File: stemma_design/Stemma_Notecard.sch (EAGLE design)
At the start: 18 parts, among them J1 MDT420E01001NOTECARD, Q2 BSS138, U2 AP2112K-3.3

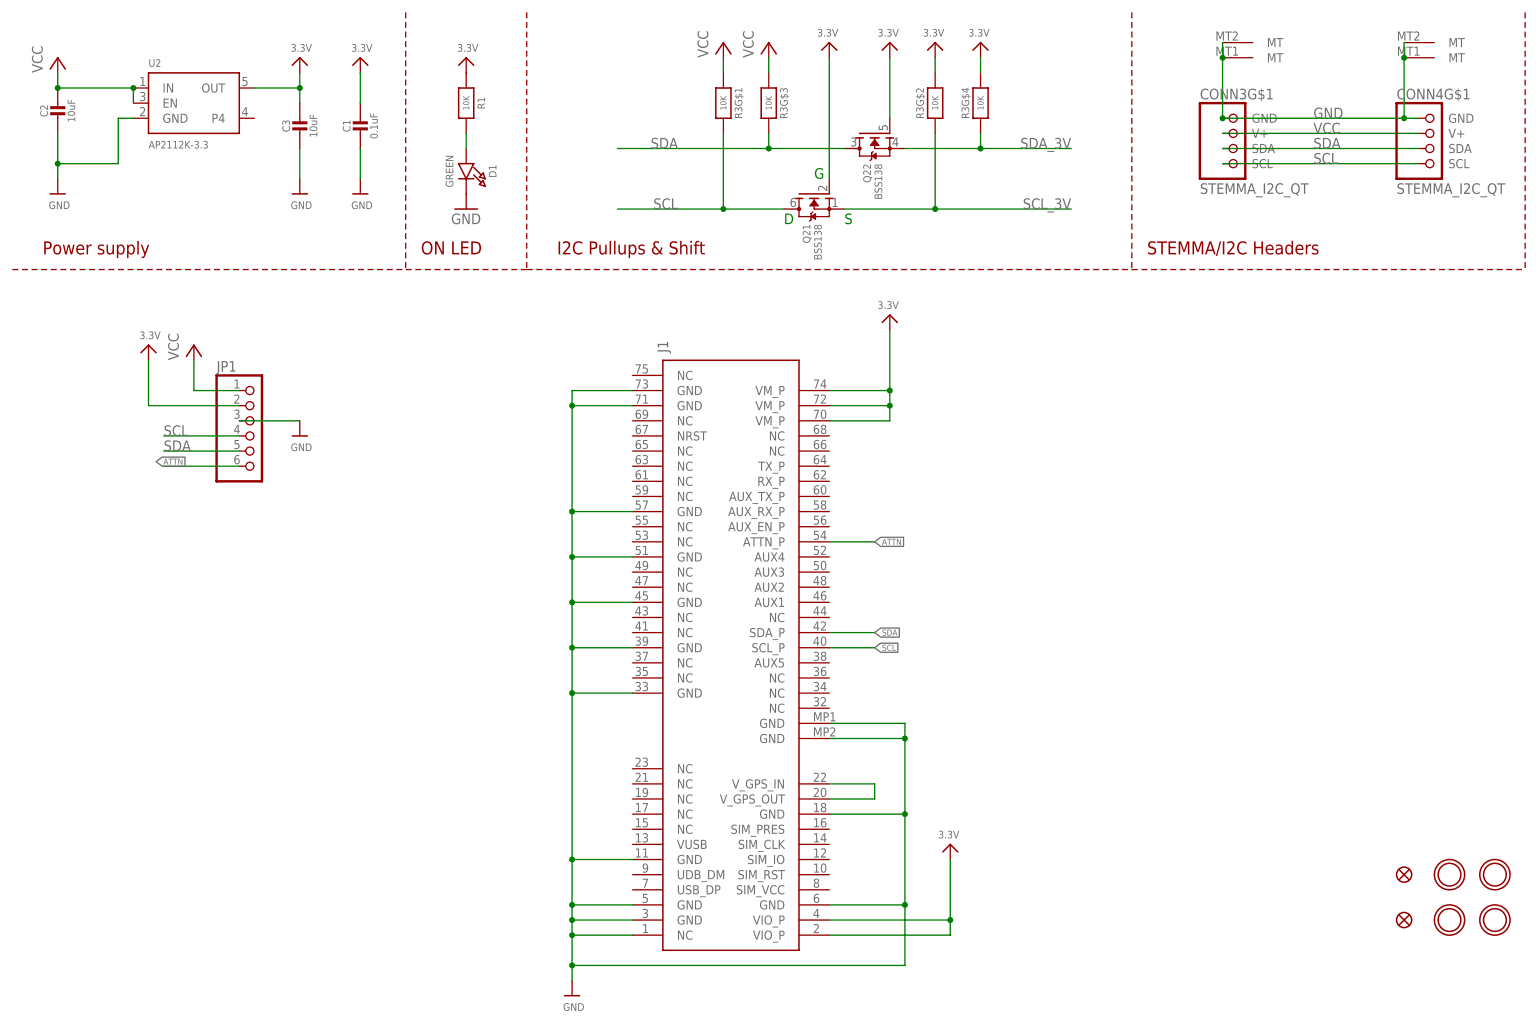
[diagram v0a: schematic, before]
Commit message: stemma design upload
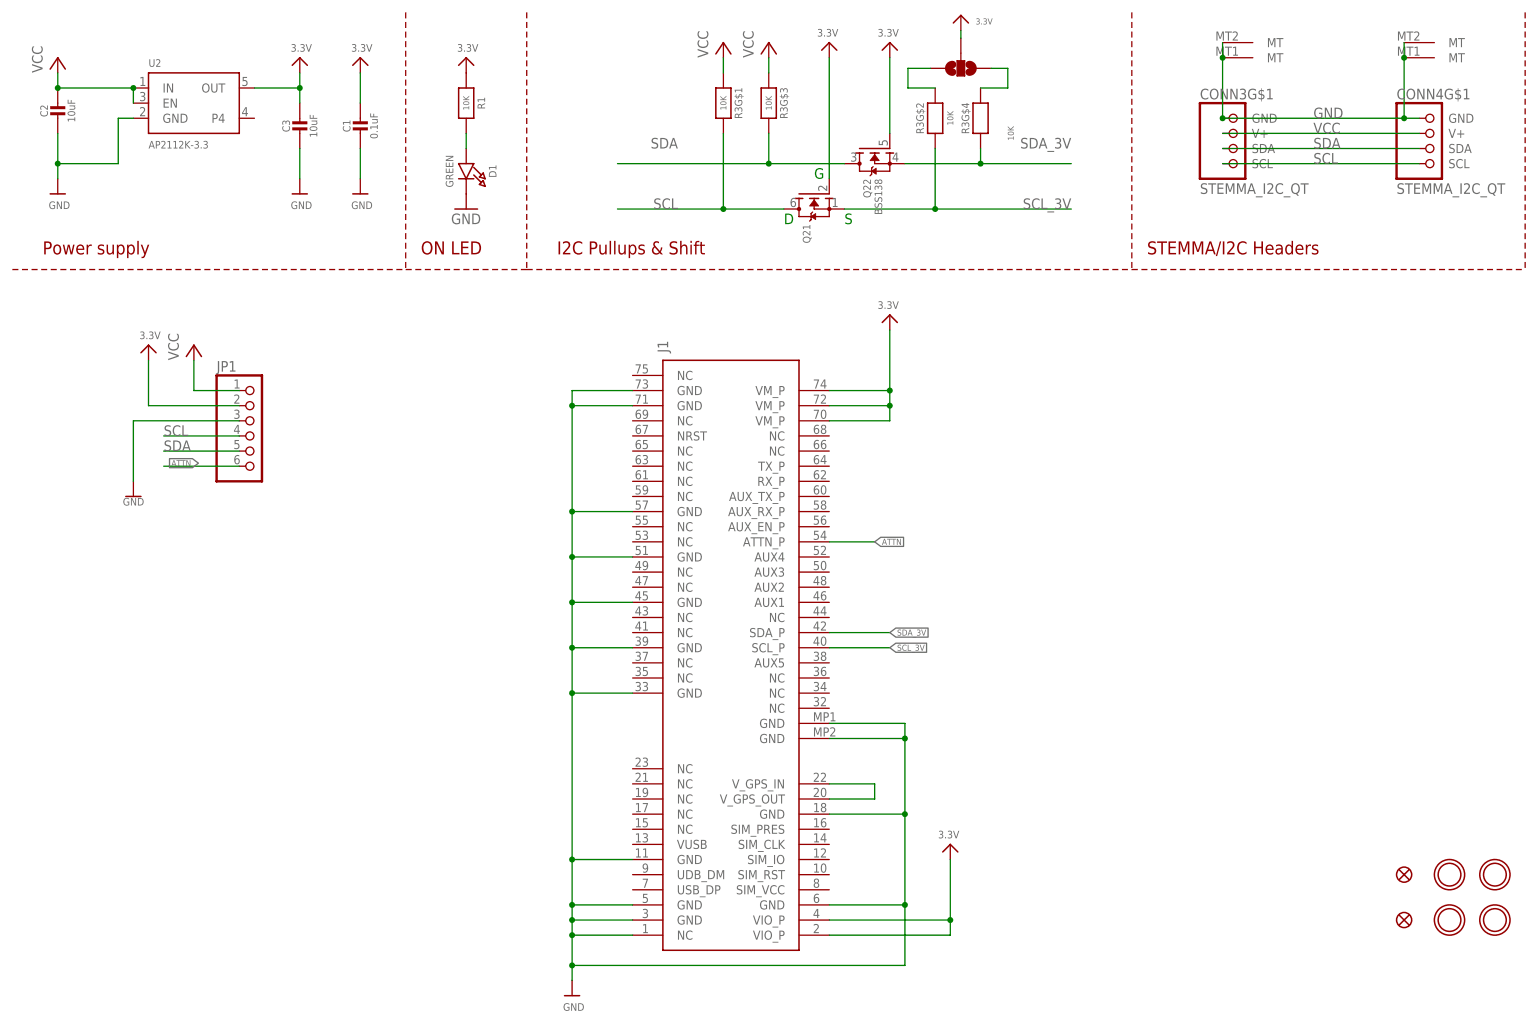
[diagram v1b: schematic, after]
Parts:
- added JP2: JUMPER-SMT_3_NO_NO-SILK, SparkFun-Jumpers:JUMPER-SMT_3_NO_NO-SILK
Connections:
- new net N$3: JP2.3, R3G$2.1
- new net N$4: JP2.1, R3G$4.1
- net 3.3V: now also JP2.2; no longer R3G$2.1, R3G$4.1
- net SCL: no longer J1.SCL_P
- net SCL_3V: now also J1.SCL_P
- net SDA: no longer J1.SDA_P
- net SDA_3V: now also J1.SDA_P
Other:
- moved on the sheet: Q22, R3G$2, R3G$4
